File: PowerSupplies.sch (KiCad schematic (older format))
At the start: 12 parts, among them U2 LM2937EM-5.0, U3 LM2937EM-5.0

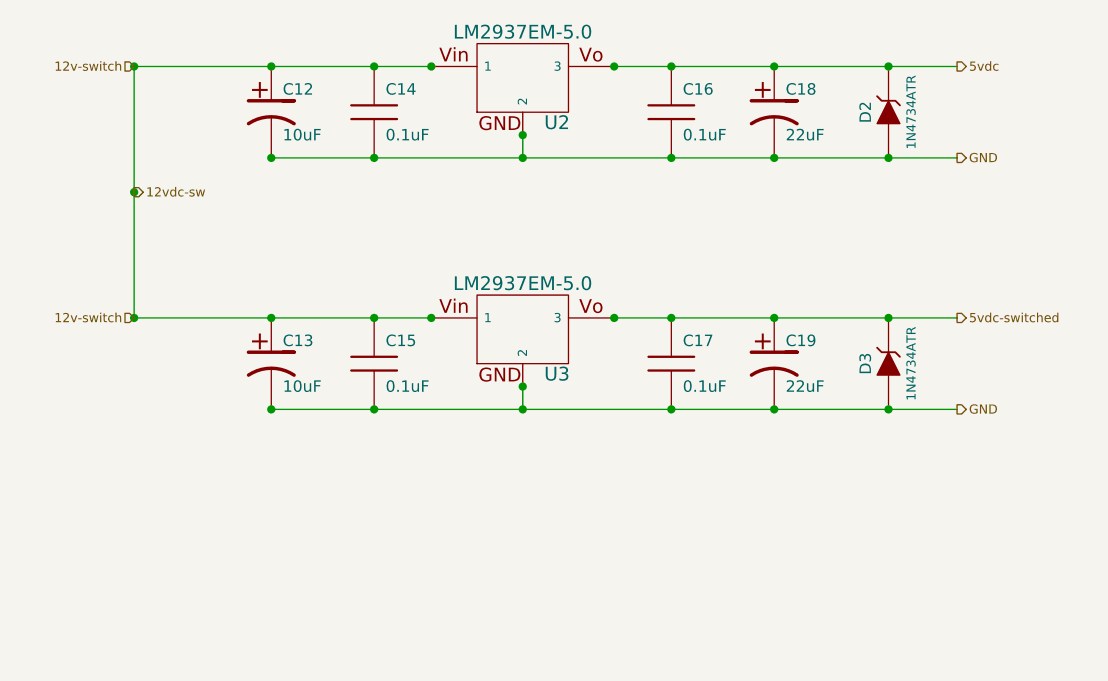
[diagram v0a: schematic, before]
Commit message: Redesigned schematics and board
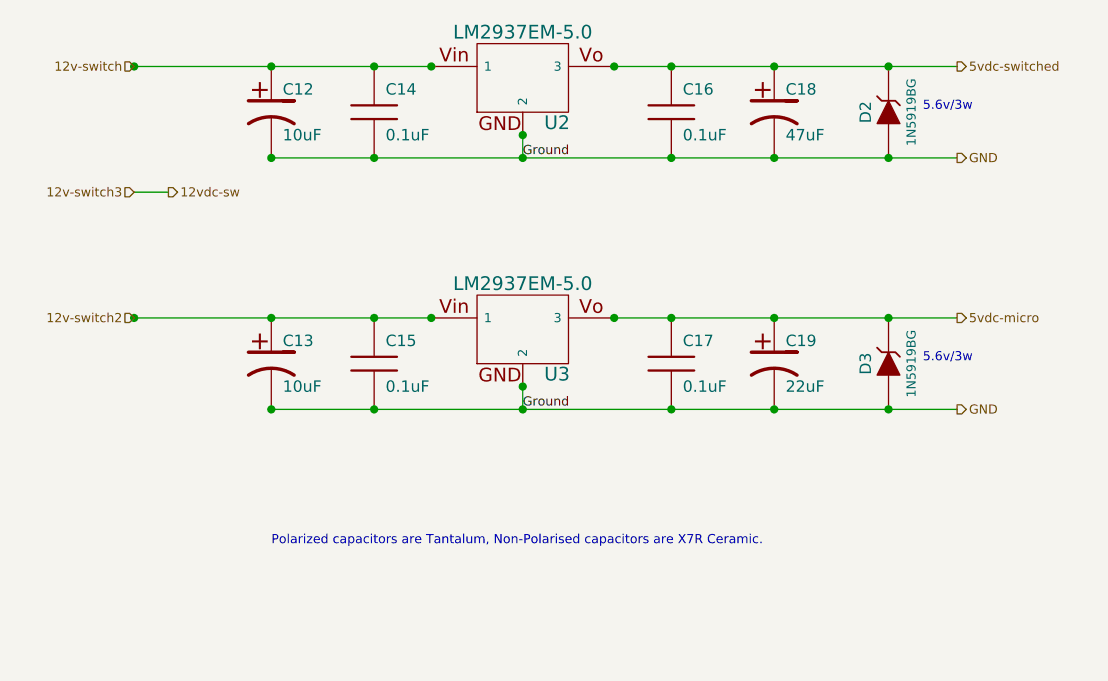
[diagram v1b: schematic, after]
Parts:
- C18: value 22uF -> 47uF
- D2, D3: value 1N4734ATR -> 1N5919BG
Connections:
- net 5vdc is gone; now on net 5vdc-switched: C16.1, C18.1, D2.2 (K), U2.3
- net 12v-switch: no longer C13.1, C15.1, U3.1
- net 5vdc-switched: no longer C17.1, C19.1, D3.2 (K), U3.3
- new net 12v-switch2: C13.1, C15.1, U3.1
- new net 5vdc-micro: C17.1, C19.1, D3.2 (K), U3.3
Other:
- note added: "5.6v/3w"
- note added: "Polarized capacitors are Tantalum, Non-Polarised capacitors are X7R Ceramic."
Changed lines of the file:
@@
-EESchema Schematic File Version 2  date Thu 19 Jan 2012 12:17:41 AM EST
+EESchema Schematic File Version 2  date Fri 20 Jan 2012 02:23:37 PM EST
 LIBS:power
 LIBS:device
@@
 Sheet 4 7
 Title ""
-Date "19 jan 2012"
+Date "20 jan 2012"
 Rev ""
 Comp ""
@@
 Comment4 ""
 $EndDescr
-Connection ~ 1750 2800
+Text Label 3450 2650 0    40   ~ 0
+Ground
+Text Label 3450 3750 0    40   ~ 0
+Ground
 Wire Wire Line
-	1750 3350 1750 2250
+	1750 2800 1900 2800
+Connection ~ 5050 3750
+Connection ~ 5050 3350
+Connection ~ 5050 2650
+Connection ~ 5050 2250
+Connection ~ 1750 2250
+Connection ~ 3450 2650
 Wire Wire Line
-	5350 3750 2350 3750
-Connection ~ 3450 3750
+	3450 2550 3450 2650
+Connection ~ 4550 3750
+Connection ~ 4550 3350
+Connection ~ 4100 3750
+Connection ~ 4100 3350
+Connection ~ 3850 3350
+Connection ~ 3450 3650
+Connection ~ 2350 3750
+Connection ~ 2800 3750
+Connection ~ 3050 3350
+Connection ~ 2800 3350
+Connection ~ 2350 3350
+Connection ~ 1750 3350
+Connection ~ 2350 2650
+Connection ~ 2800 2650
+Connection ~ 3450 2550
+Connection ~ 4100 2650
+Connection ~ 4550 2650
+Connection ~ 4550 2250
+Connection ~ 4100 2250
+Connection ~ 3850 2250
+Connection ~ 3050 2250
+Connection ~ 2800 2250
+Connection ~ 2350 2250
 Wire Wire Line
-	3450 3650 3450 3750
+	3850 3350 5350 3350
+Wire Wire Line
+	3850 2250 5350 2250
+Wire Wire Line
+	1750 2250 3050 2250
+Wire Wire Line
+	2350 2650 5350 2650
 Wire Wire Line
 	1750 3350 3050 3350
 Wire Wire Line
-	2350 2650 5350 2650
+	3450 3650 3450 3750
+Connection ~ 3450 3750
 Wire Wire Line
-	1750 2250 3050 2250
-Wire Wire Line
-	3850 2250 5350 2250
-Wire Wire Line
-	3850 3350 5350 3350
-Connection ~ 2350 2250
-Connection ~ 2800 2250
-Connection ~ 3050 2250
-Connection ~ 3850 2250
-Connection ~ 4100 2250
-Connection ~ 4550 2250
-Connection ~ 4550 2650
-Connection ~ 4100 2650
-Connection ~ 3450 2550
-Connection ~ 2800 2650
-Connection ~ 2350 2650
-Connection ~ 1750 3350
-Connection ~ 2350 3350
-Connection ~ 2800 3350
-Connection ~ 3050 3350
-Connection ~ 2800 3750
-Connection ~ 2350 3750
-Connection ~ 3450 3650
-Connection ~ 3850 3350
-Connection ~ 4100 3350
-Connection ~ 4100 3750
-Connection ~ 4550 3350
-Connection ~ 4550 3750
-Wire Wire Line
-	3450 2550 3450 2650
-Connection ~ 3450 2650
-Connection ~ 1750 2250
-Connection ~ 5050 2250
-Connection ~ 5050 2650
-Connection ~ 5050 3350
-Connection ~ 5050 3750
-Text HLabel 1750 2800 2    40   Output ~ 0
+	5350 3750 2350 3750
+Text HLabel 1750 2800 0    40   Input ~ 0
+12v-switch3
+Text HLabel 1750 3350 0    40   Input ~ 0
+12v-switch2
+Text Notes 2350 4350 0    40   ~ 0
+Polarized capacitors are Tantalum, Non-Polarised capacitors are X7R Ceramic.
+Text Notes 5200 3550 0    40   ~ 0
+5.6v/3w
+Text Notes 5200 2450 0    40   ~ 0
+5.6v/3w
+Text HLabel 1900 2800 2    40   Output ~ 0
 12vdc-sw
 $Comp
@@
 P 5050 3550
 F 0 "D3" H 5050 3650 50  0000 C CNN
-F 1 "1N4734ATR" H 5050 3450 40  0000 C CNN
+F 1 "1N5919BG" H 5050 3450 40  0000 C CNN
 	1    5050 3550
 	0    -1   -1   0
@@
 P 5050 2450
 F 0 "D2" H 5050 2550 50  0000 C CNN
-F 1 "1N4734ATR" H 5050 2350 40  0000 C CNN
+F 1 "1N5919BG" H 5050 2350 40  0000 C CNN
 	1    5050 2450
 	0    -1   -1   0
 $EndComp
-Text HLabel 1750 3350 0    40   Input ~ 0
-12v-switch
 Text HLabel 1750 2250 0    40   Input ~ 0
 12v-switch
@@
 	1    0    0    -1
 $EndComp
-Text HLabel 5350 3350 2    40   Output ~ 0
+Text HLabel 5350 2250 2    40   Output ~ 0
 5vdc-switched
 Text HLabel 5350 2650 2    40   Output ~ 0
 GND
-Text HLabel 5350 2250 2    40   Output ~ 0
-5vdc
+Text HLabel 5350 3350 2    40   Output ~ 0
+5vdc-micro
 $Comp
 L CP1 C18
@@
 P 4550 2450
 F 0 "C18" H 4600 2550 50  0000 L CNN
-F 1 "22uF" H 4600 2350 50  0000 L CNN
+F 1 "47uF" H 4600 2350 50  0000 L CNN
 	1    4550 2450
 	1    0    0    -1

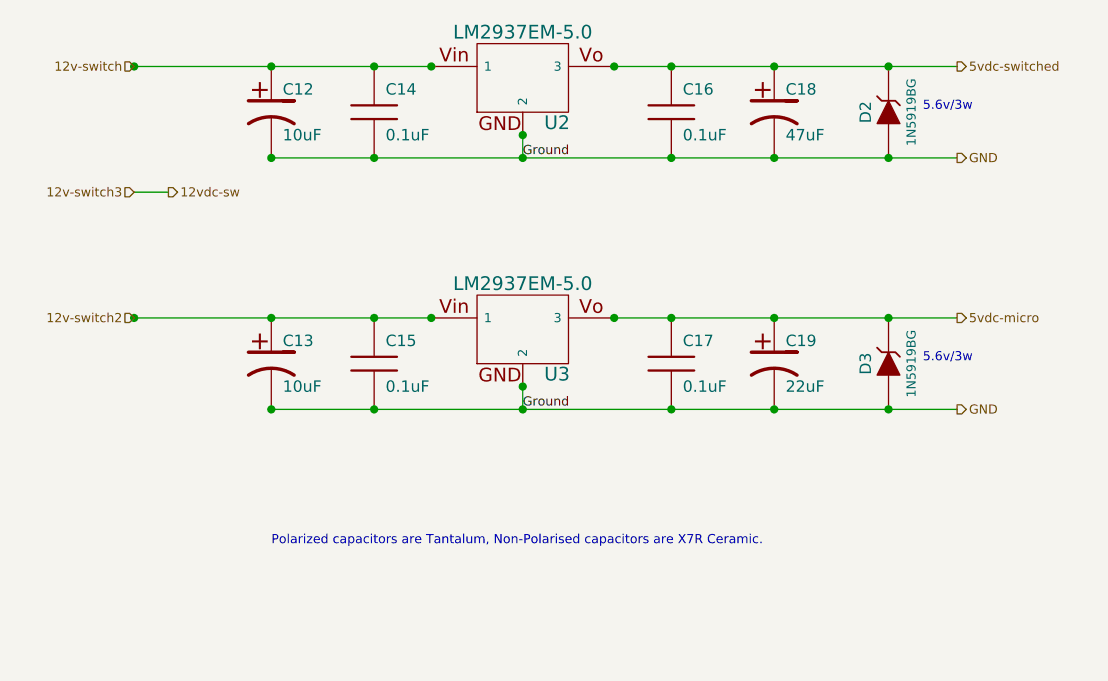
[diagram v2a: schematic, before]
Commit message: Modified: schematics to correct errors
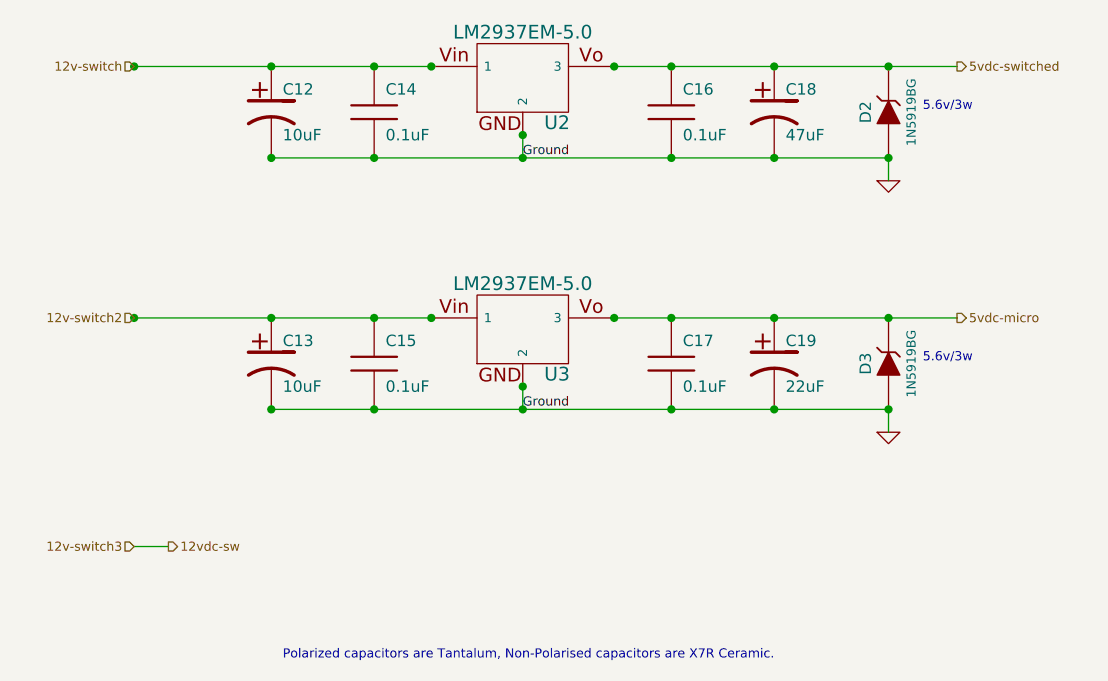
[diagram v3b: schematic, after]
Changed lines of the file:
@@
-EESchema Schematic File Version 2  date Sun 22 Jan 2012 12:58:37 AM EST
+EESchema Schematic File Version 2  date Sun 22 Jan 2012 05:59:51 PM EST
 LIBS:power
 LIBS:device
@@
 Comment4 ""
 $EndDescr
-Text Label 3450 2650 0    40   ~ 0
-Ground
-Text Label 3450 3750 0    40   ~ 0
-Ground
 Wire Wire Line
-	1750 2800 1900 2800
+	1750 4350 1900 4350
 Connection ~ 5050 3750
 Connection ~ 5050 3350
@@
 	1750 2250 3050 2250
 Wire Wire Line
-	2350 2650 5350 2650
+	2350 2650 5050 2650
 Wire Wire Line
 	1750 3350 3050 3350
@@
 Connection ~ 3450 3750
 Wire Wire Line
-	5350 3750 2350 3750
-Text HLabel 1750 2800 0    40   Input ~ 0
+	2350 3750 5050 3750
+Wire Wire Line
+	5050 2650 5050 2750
+Wire Wire Line
+	5050 3750 5050 3850
+$Comp
+L GND #PWR24
+U 1 1 4F1C2CDE
+P 5050 3850
+F 0 "#PWR24" H 5050 3850 30  0001 C CNN
+F 1 "GND" H 5050 3780 30  0001 C CNN
+	1    5050 3850
+	1    0    0    -1
+$EndComp
+$Comp
+L GND #PWR23
+U 1 1 4F1C2CC1
+P 5050 2750
+F 0 "#PWR23" H 5050 2750 30  0001 C CNN
+F 1 "GND" H 5050 2680 30  0001 C CNN
+	1    5050 2750
+	1    0    0    -1
+$EndComp
+Text Label 3450 2650 0    40   ~ 0
+Ground
+Text Label 3450 3750 0    40   ~ 0
+Ground
+Text HLabel 1750 4350 0    40   Input ~ 0
 12v-switch3
 Text HLabel 1750 3350 0    40   Input ~ 0
 12v-switch2
-Text Notes 2350 4350 0    40   ~ 0
+Text Notes 2400 4850 0    40   ~ 0
 Polarized capacitors are Tantalum, Non-Polarised capacitors are X7R Ceramic.
 Text Notes 5200 3550 0    40   ~ 0
@@
 Text Notes 5200 2450 0    40   ~ 0
 5.6v/3w
-Text HLabel 1900 2800 2    40   Output ~ 0
+Text HLabel 1900 4350 2    40   Output ~ 0
 12vdc-sw
 $Comp
@@
 Text HLabel 1750 2250 0    40   Input ~ 0
 12v-switch
-Text HLabel 5350 3750 2    40   Output ~ 0
-GND
 $Comp
 L CP1 C13
@@
 Text HLabel 5350 2250 2    40   Output ~ 0
 5vdc-switched
-Text HLabel 5350 2650 2    40   Output ~ 0
-GND
 Text HLabel 5350 3350 2    40   Output ~ 0
 5vdc-micro

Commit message: Improved schematic, re-design board, re-created PDF
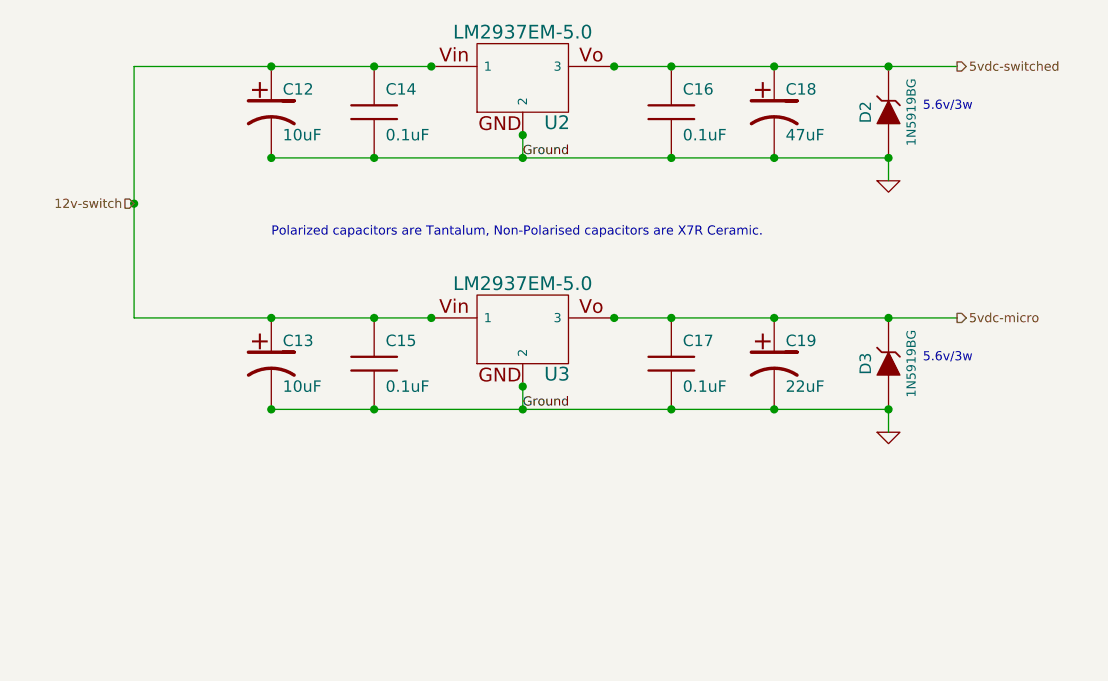
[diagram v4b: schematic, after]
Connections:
- net 12v-switch2 is gone; now on net 12v-switch: C13.1, C15.1, U3.1
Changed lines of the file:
@@
-EESchema Schematic File Version 2  date Sun 22 Jan 2012 05:59:51 PM EST
+EESchema Schematic File Version 2  date Mon 23 Jan 2012 07:28:42 AM EST
 LIBS:power
 LIBS:device
@@
 EELAYER END
 $Descr A4 11700 8267
-Sheet 4 7
-Title ""
-Date "22 jan 2012"
-Rev ""
-Comp ""
+Sheet 5 7
+Title "Jaguar PCB for FreeEMS"
+Date "23 jan 2012"
+Rev "A.1"
+Comp "diyefi.org"
 Comment1 ""
 Comment2 ""
@@
 Comment4 ""
 $EndDescr
+Connection ~ 1750 2850
 Wire Wire Line
-	1750 4350 1900 4350
-Connection ~ 5050 3750
-Connection ~ 5050 3350
-Connection ~ 5050 2650
-Connection ~ 5050 2250
-Connection ~ 1750 2250
-Connection ~ 3450 2650
+	1750 3350 1750 2250
 Wire Wire Line
-	3450 2550 3450 2650
-Connection ~ 4550 3750
-Connection ~ 4550 3350
-Connection ~ 4100 3750
-Connection ~ 4100 3350
-Connection ~ 3850 3350
-Connection ~ 3450 3650
-Connection ~ 2350 3750
-Connection ~ 2800 3750
-Connection ~ 3050 3350
-Connection ~ 2800 3350
-Connection ~ 2350 3350
-Connection ~ 1750 3350
-Connection ~ 2350 2650
-Connection ~ 2800 2650
-Connection ~ 3450 2550
-Connection ~ 4100 2650
-Connection ~ 4550 2650
-Connection ~ 4550 2250
-Connection ~ 4100 2250
-Connection ~ 3850 2250
-Connection ~ 3050 2250
-Connection ~ 2800 2250
-Connection ~ 2350 2250
+	5050 3850 5050 3750
 Wire Wire Line
-	3850 3350 5350 3350
+	5050 2750 5050 2650
+Wire Wire Line
+	5050 3750 2350 3750
+Connection ~ 3450 3750
+Wire Wire Line
+	3450 3650 3450 3750
+Wire Wire Line
+	1750 3350 3050 3350
+Wire Wire Line
+	5050 2650 2350 2650
+Wire Wire Line
+	1750 2250 3050 2250
 Wire Wire Line
 	3850 2250 5350 2250
 Wire Wire Line
-	1750 2250 3050 2250
+	3850 3350 5350 3350
+Connection ~ 2350 2250
+Connection ~ 2800 2250
+Connection ~ 3050 2250
+Connection ~ 3850 2250
+Connection ~ 4100 2250
+Connection ~ 4550 2250
+Connection ~ 4550 2650
+Connection ~ 4100 2650
+Connection ~ 3450 2550
+Connection ~ 2800 2650
+Connection ~ 2350 2650
+Connection ~ 2350 3350
+Connection ~ 2800 3350
+Connection ~ 3050 3350
+Connection ~ 2800 3750
+Connection ~ 2350 3750
+Connection ~ 3450 3650
+Connection ~ 3850 3350
+Connection ~ 4100 3350
+Connection ~ 4100 3750
+Connection ~ 4550 3350
+Connection ~ 4550 3750
 Wire Wire Line
-	2350 2650 5050 2650
-Wire Wire Line
-	1750 3350 3050 3350
-Wire Wire Line
-	3450 3650 3450 3750
-Connection ~ 3450 3750
-Wire Wire Line
-	2350 3750 5050 3750
-Wire Wire Line
-	5050 2650 5050 2750
-Wire Wire Line
-	5050 3750 5050 3850
+	3450 2550 3450 2650
+Connection ~ 3450 2650
+Connection ~ 5050 2250
+Connection ~ 5050 2650
+Connection ~ 5050 3350
+Connection ~ 5050 3750
+Text HLabel 1750 2850 0    40   Input ~ 0
+12v-switch
 $Comp
-L GND #PWR24
+L GND #PWR031
 U 1 1 4F1C2CDE
 P 5050 3850
-F 0 "#PWR24" H 5050 3850 30  0001 C CNN
+F 0 "#PWR031" H 5050 3850 30  0001 C CNN
 F 1 "GND" H 5050 3780 30  0001 C CNN
 	1    5050 3850
@@
 $EndComp
 $Comp
-L GND #PWR23
+L GND #PWR032
 U 1 1 4F1C2CC1
 P 5050 2750
-F 0 "#PWR23" H 5050 2750 30  0001 C CNN
+F 0 "#PWR032" H 5050 2750 30  0001 C CNN
 F 1 "GND" H 5050 2680 30  0001 C CNN
 	1    5050 2750
@@
 Text Label 3450 3750 0    40   ~ 0
 Ground
-Text HLabel 1750 4350 0    40   Input ~ 0
-12v-switch3
-Text HLabel 1750 3350 0    40   Input ~ 0
-12v-switch2
-Text Notes 2400 4850 0    40   ~ 0
+Text Notes 2350 3000 0    40   ~ 0
 Polarized capacitors are Tantalum, Non-Polarised capacitors are X7R Ceramic.
 Text Notes 5200 3550 0    40   ~ 0
@@
 Text Notes 5200 2450 0    40   ~ 0
 5.6v/3w
-Text HLabel 1900 4350 2    40   Output ~ 0
-12vdc-sw
 $Comp
 L ZENER D3
@@
 	0    -1   -1   0
 $EndComp
-Text HLabel 1750 2250 0    40   Input ~ 0
-12v-switch
 $Comp
 L CP1 C13
